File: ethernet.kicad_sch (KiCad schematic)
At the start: 70 parts, among them Q5001 DMG1012T, Q5002 DMG1012T, U1002 AM6231ASGGGAALW, U5001 HR911130A, U5002 RTL8211F-CG, U5003 TPD4E05U06DQA, U5004 TPD4E05U06DQA

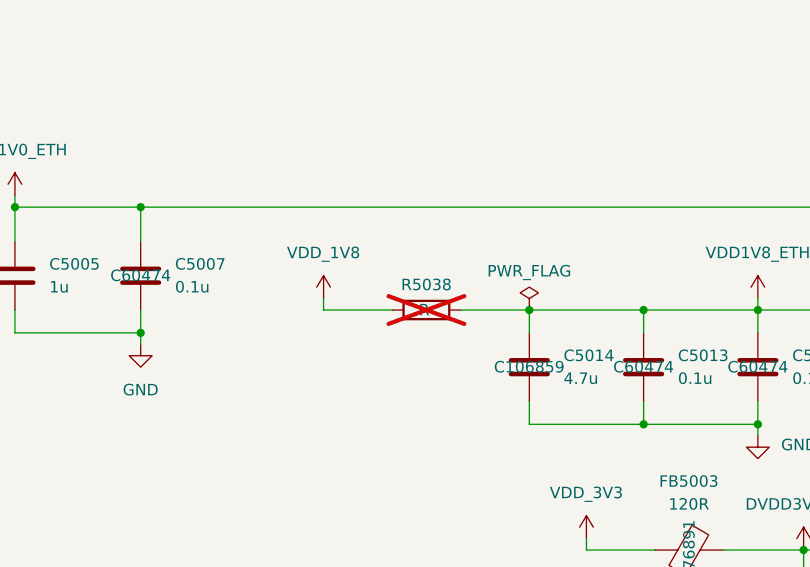
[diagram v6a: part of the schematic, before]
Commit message: Finished Ethernet routing
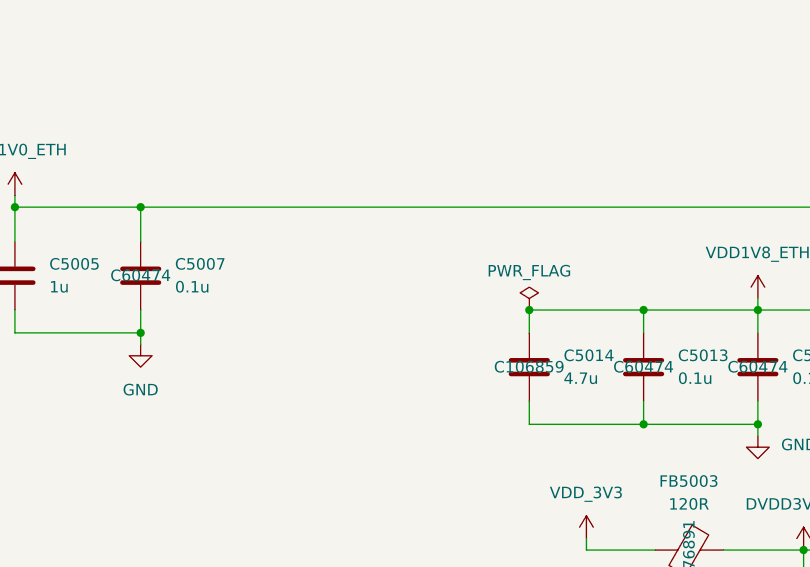
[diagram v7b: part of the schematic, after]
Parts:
- removed R5038: R, Resistor_SMD:R_0402_1005Metric, symbol Device:R
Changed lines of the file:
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@@
 	(wire
 		(pts
-			(xy 203.2 130.81) (xy 210.82 130.81)
-		)
-		(stroke
-			(width 0)
-			(type default)
-		)
-	)
-	(wire
-		(pts
 			(xy 435.61 151.13) (xy 435.61 149.86)
 		)
@@
 	(wire
 		(pts
-			(xy 218.44 130.81) (xy 226.06 130.81)
-		)
-		(stroke
-			(width 0)
-			(type default)
-		)
-	)
-	(wire
-		(pts
 			(xy 464.82 251.46) (xy 464.82 252.73)
 		)
@@
 	(wire
 		(pts
-			(xy 203.2 129.54) (xy 203.2 130.81)
-		)
-		(stroke
-			(width 0)
-			(type default)
-		)
-	)
-	(wire
-		(pts
 			(xy 204.47 323.85) (xy 204.47 331.47)
 		)
@@
 	(symbol
 		(lib_id "power:VDD")
-		(at 203.2 129.54 0)
-		(unit 1)
-		(exclude_from_sim no)
-		(in_bom yes)
-		(on_board yes)
-		(dnp no)
-		(fields_autoplaced yes)
-		(property "Reference" "#PWR05010"
-			(at 203.2 133.35 0)
-			(effects
-				(font
-					(size 1.27 1.27)
-				)
-				(hide yes)
-			)
-		)
-		(property "Value" "VDD_1V8"
-			(at 203.2 124.46 0)
-			(effects
-				(font
-					(size 1.27 1.27)
-				)
-			)
-		)
-		(property "Footprint" ""
-			(at 203.2 129.54 0)
-			(effects
-				(font
-					(size 1.27 1.27)
-				)
-				(hide yes)
-			)
-		)
-		(property "Datasheet" ""
-			(at 203.2 129.54 0)
-			(effects
-				(font
-					(size 1.27 1.27)
-				)
-				(hide yes)
-			)
-		)
-		(property "Description" "Power symbol creates a global label with name \"VDD\""
-			(at 203.2 129.54 0)
-			(effects
-				(font
-					(size 1.27 1.27)
-				)
-				(hide yes)
-			)
-		)
-		(pin "1"
-		)
-		(instances
-			(project ""
-				(path "/b43b7bca-e50d-42ec-8ff0-e0016dfefe0a/6c7f2037-3077-4980-ab71-7ff032fdfd6e"
-					(reference "#PWR05010")
-					(unit 1)
-				)
-			)
-		)
-	)
-	(symbol
-		(lib_id "power:VDD")
 		(at 396.24 93.98 0)
 		(mirror y)
@@
 					(unit 1)
 				)
-			)
-		)
-	)
-	(symbol
-		(lib_id "Device:R")
-		(at 214.63 130.81 90)
-		(unit 1)
-		(exclude_from_sim no)
-		(in_bom yes)
-		(on_board yes)
-		(dnp yes)
-		(property "Reference" "R5038"
-			(at 214.63 128.016 90)
-			(effects
-				(font
-					(size 1.27 1.27)
-				)
-			)
-		)
-		(property "Value" "R"
-			(at 214.376 130.81 90)
-			(effects
-				(font
-					(size 1.27 1.27)
-				)
-			)
-		)
-		(property "Footprint" "Resistor_SMD:R_0402_1005Metric"
-			(at 214.63 132.588 90)
-			(effects
-				(font
-					(size 1.27 1.27)
-				)
-				(hide yes)
-			)
-		)
-		(property "Datasheet" "~"
-			(at 214.63 130.81 0)
-			(effects
-				(font
-					(size 1.27 1.27)
-				)
-				(hide yes)
-			)
-		)
-		(property "Description" "Resistor"
-			(at 214.63 130.81 0)
-			(effects
-				(font
-					(size 1.27 1.27)
-				)
-				(hide yes)
-			)
-		)
-		(pin "2"
-		)
-		(pin "1"
-		)
-		(instances
-			(project ""
-				(path "/b43b7bca-e50d-42ec-8ff0-e0016dfefe0a/6c7f2037-3077-4980-ab71-7ff032fdfd6e"
-					(reference "R5038")
-					(unit 1)
-				)

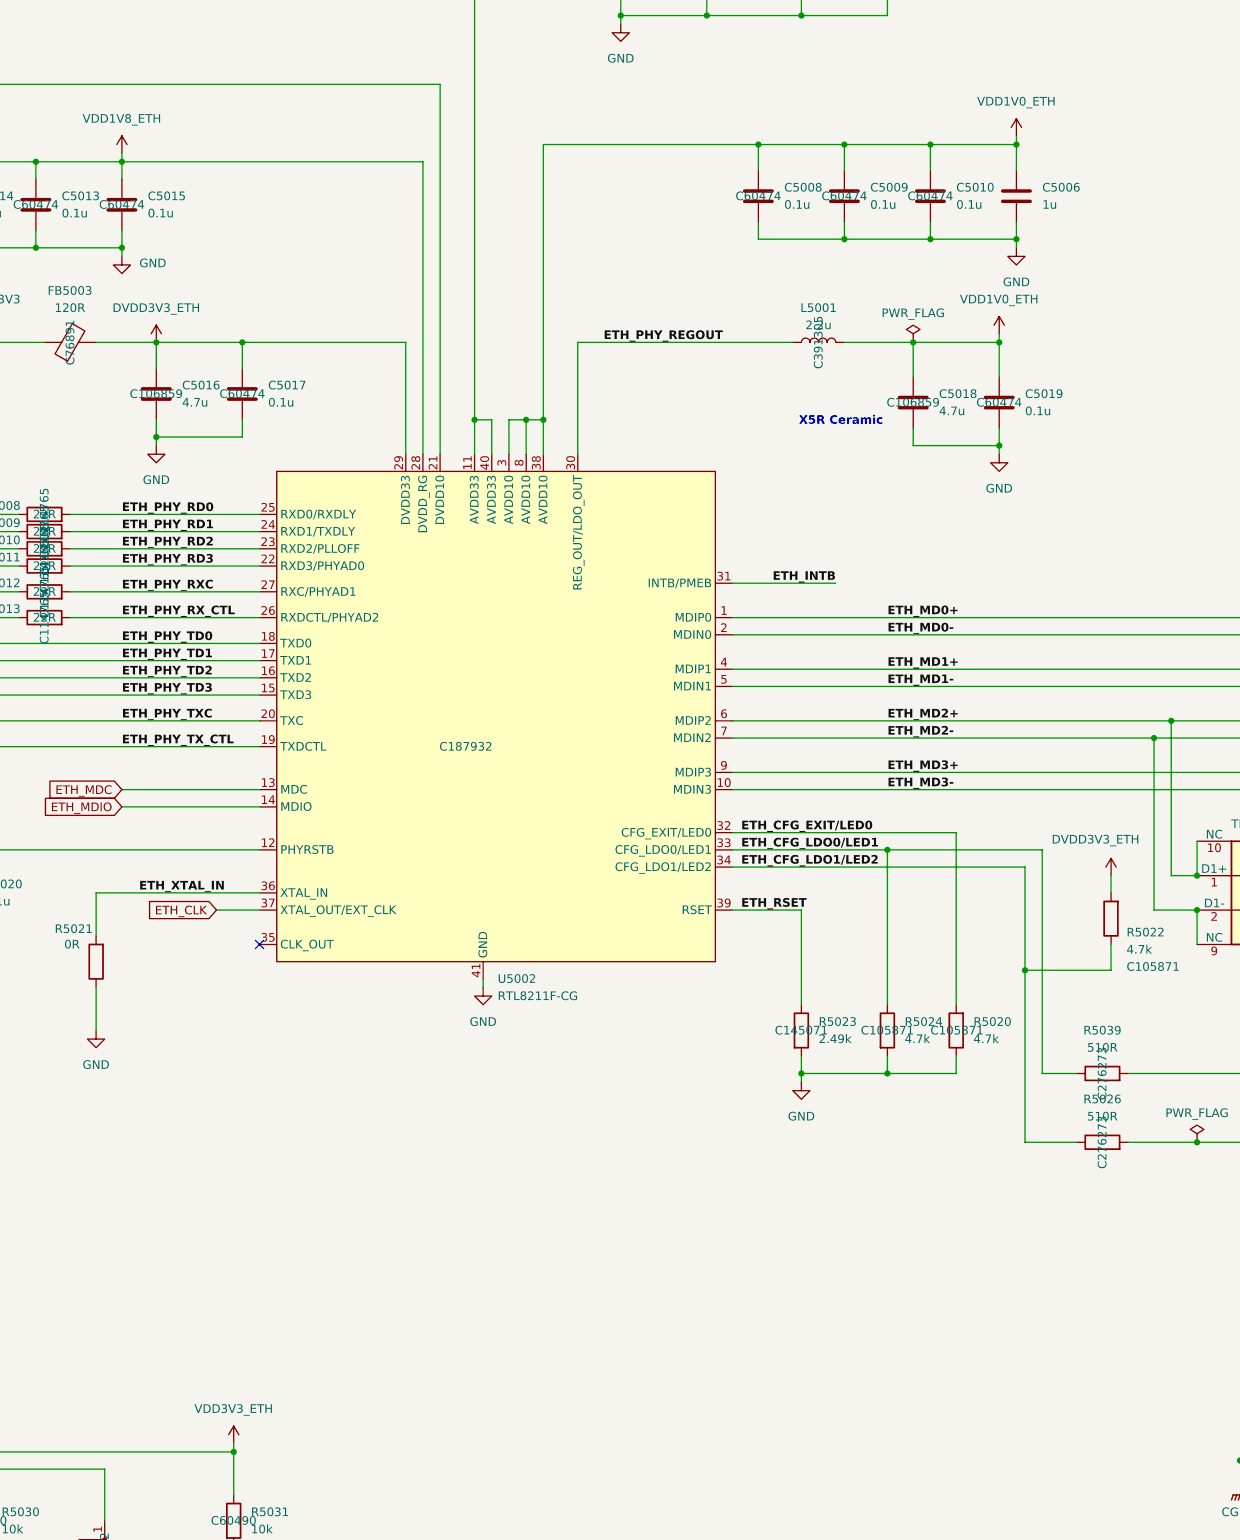
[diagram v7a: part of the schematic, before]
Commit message: Fixed Ethernet inductor and capacitor regulator parts. Cleaned up Ethernet routing
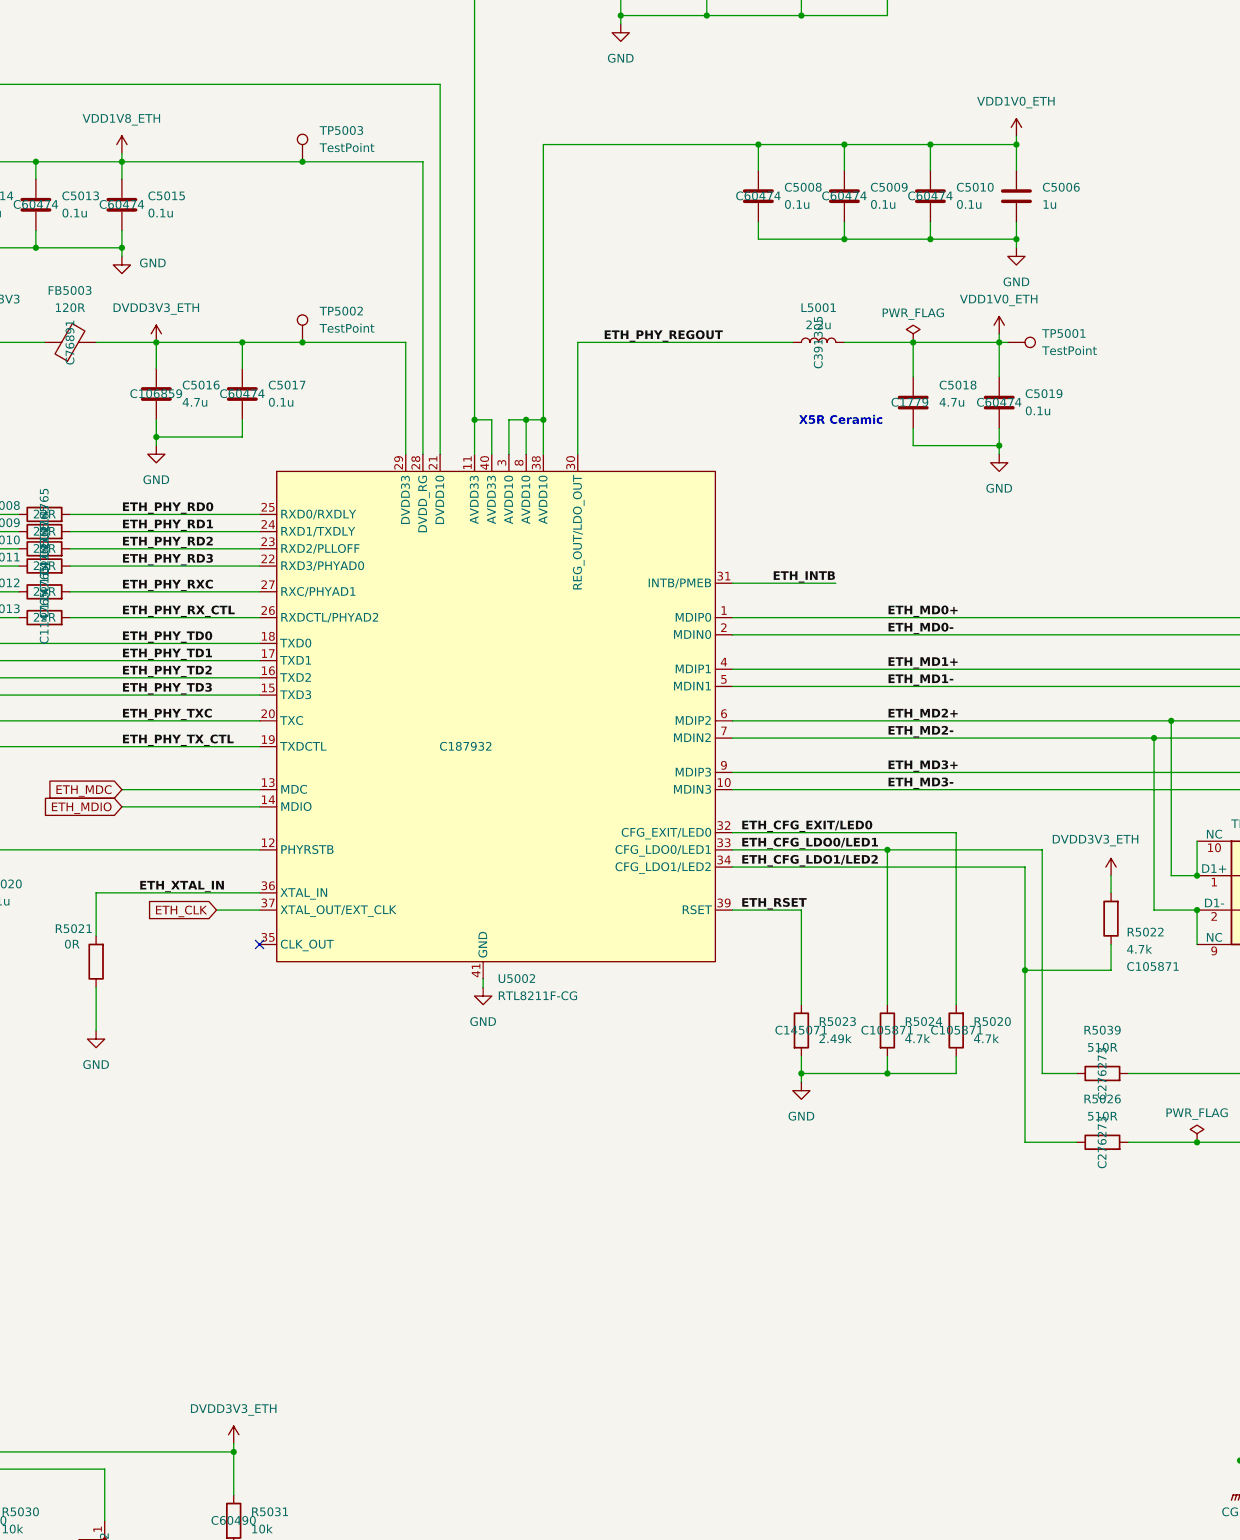
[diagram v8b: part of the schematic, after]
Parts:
- added TP5001, TP5002, TP5003: TestPoint, TestPoint:TestPoint_Pad_1.0x1.0mm, symbol Connector:TestPoint
- C5018: footprint Capacitor_SMD:C_0402_1005Metric -> Capacitor_SMD:C_0805_2012Metric; JLCPCB Part# C106859 -> C1779
- L5001: footprint SoftServicesFootprintLibrary:CVH201610A-2R2M -> DFE252012P-2R2M=P2:DFE2HCAH1R0MJ0L
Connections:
- net VDD3V3_ETH is gone; now on net DVDD3V3_ETH: R5029.1, R5031.1
- net DVDD3V3_ETH: now also TP5002.1
- net VDD1V0_ETH: now also TP5001.1
- net VDD1V8_ETH: now also TP5003.1
